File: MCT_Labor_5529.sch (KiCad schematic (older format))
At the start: 0 parts

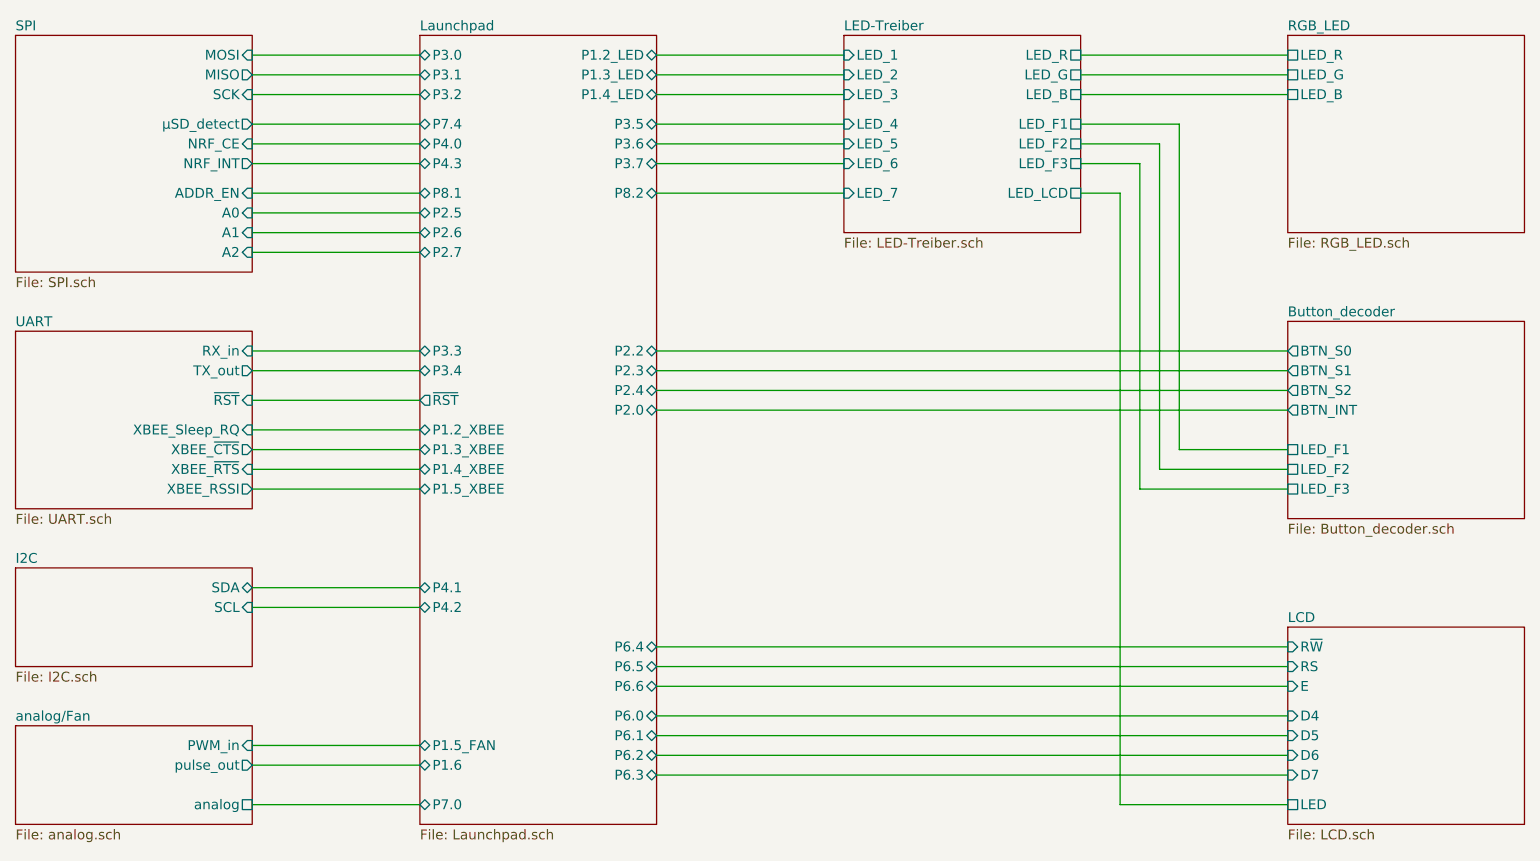
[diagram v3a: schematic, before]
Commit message: Anpassungen am Lüfteranschluss und den LEDs
-Lüfteranschluss verändert
 -> 12V-Versorgung eingefügt
-LED & LCD auf 3,3V umgestellt
 -> Ladungspunpe für neg. Kontrastspannung
-keine 5V Versorgung mehr
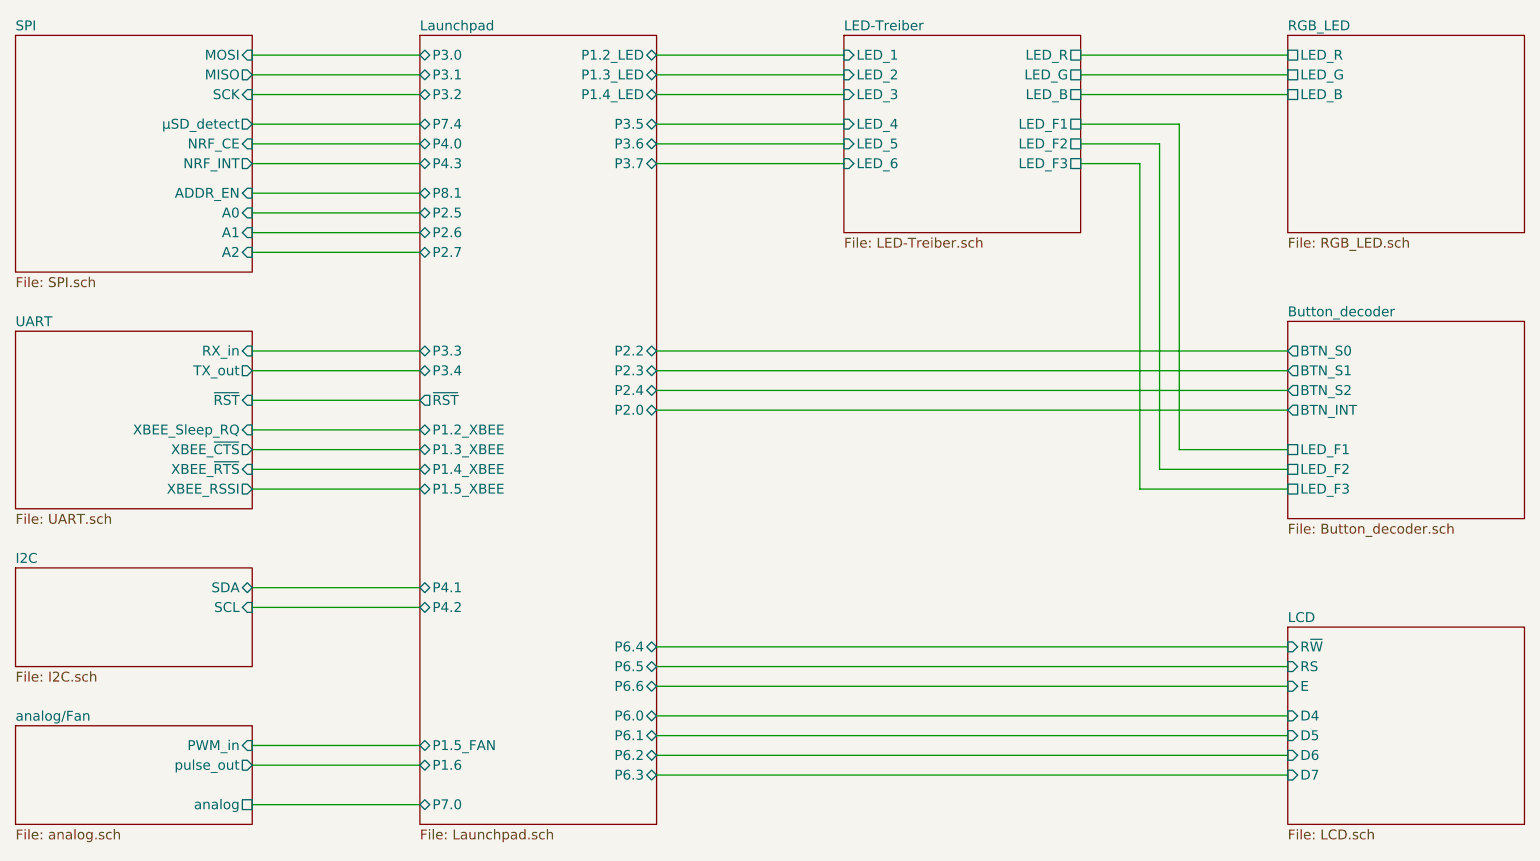
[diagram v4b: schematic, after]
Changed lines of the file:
@@
 F7 "R~W~" I L 8750 4650 50
 F8 "E" I L 8750 4850 50
-F9 "LED" U L 8750 5450 50
 $EndSheet
 Wire Wire Line
@@
 F6 "LED_5" I L 6500 2100 50
 F7 "LED_6" I L 6500 2200 50
-F8 "LED_7" I L 6500 2350 50
-F9 "LED_R" U R 7700 1650 50
-F10 "LED_G" U R 7700 1750 50
-F11 "LED_B" U R 7700 1850 50
-F12 "LED_F1" U R 7700 2000 50
-F13 "LED_F2" U R 7700 2100 50
-F14 "LED_F3" U R 7700 2200 50
-F15 "LED_LCD" U R 7700 2350 50
-$EndSheet
-Wire Wire Line
-	7700 2350 7900 2350
-Wire Wire Line
-	7900 2350 7900 5450
-Wire Wire Line
-	7900 5450 8750 5450
+F8 "LED_R" U R 7700 1650 50
+F9 "LED_G" U R 7700 1750 50
+F10 "LED_B" U R 7700 1850 50
+F11 "LED_F1" U R 7700 2000 50
+F12 "LED_F2" U R 7700 2100 50
+F13 "LED_F3" U R 7700 2200 50
+$EndSheet
 Wire Wire Line
 	6500 1650 5550 1650
@@
 Wire Wire Line
 	5550 2200 6500 2200
-Wire Wire Line
-	5550 2350 6500 2350
 $Sheet
 S 8750 3000 1200 1000
@@
 F14 "P4.0" B L 4350 2100 50
 F15 "P3.7" B R 5550 2200 50
-F16 "P8.2" B R 5550 2350 50
-F17 "P6.0" B R 5550 5000 50
-F18 "P6.1" B R 5550 5100 50
-F19 "P6.2" B R 5550 5200 50
-F20 "P6.3" B R 5550 5300 50
-F21 "P6.4" B R 5550 4650 50
-F22 "P7.0" B L 4350 5450 50
-F23 "P3.6" B R 5550 2100 50
-F24 "P3.5" B R 5550 2000 50
-F25 "P2.0" B R 5550 3450 50
-F26 "P2.2" B R 5550 3150 50
-F27 "P7.4" B L 4350 2000 50
-F28 "P3.0" B L 4350 1650 50
-F29 "P3.1" B L 4350 1750 50
-F30 "P2.6" B L 4350 2550 50
-F31 "P2.3" B R 5550 3250 50
-F32 "P8.1" B L 4350 2350 50
-F33 "~RST" O L 4350 3400 50
-F34 "P1.4_LED" B R 5550 1850 50
-F35 "P1.3_LED" B R 5550 1750 50
-F36 "P1.2_LED" B R 5550 1650 50
-F37 "P1.2_XBEE" B L 4350 3550 50
-F38 "P1.3_XBEE" B L 4350 3650 50
-F39 "P1.4_XBEE" B L 4350 3750 50
-F40 "P1.5_FAN" B L 4350 5150 50
-F41 "P1.5_XBEE" B L 4350 3850 50
-$EndSheet
-Wire Wire Line
+F16 "P6.0" B R 5550 5000 50
+F17 "P6.1" B R 5550 5100 50
+F18 "P6.2" B R 5550 5200 50
+F19 "P6.3" B R 5550 5300 50
+F20 "P6.4" B R 5550 4650 50
+F21 "P7.0" B L 4350 5450 50
+F22 "P3.6" B R 5550 2100 50
+F23 "P3.5" B R 5550 2000 50
+F24 "P2.0" B R 5550 3450 50
+F25 "P2.2" B R 5550 3150 50
+F26 "P7.4" B L 4350 2000 50
+F27 "P3.0" B L 4350 1650 50
+F28 "P3.1" B L 4350 1750 50
+F29 "P2.6" B L 4350 2550 50
+F30 "P2.3" B R 5550 3250 50
+F31 "P8.1" B L 4350 2350 50
+F32 "~RST" O L 4350 3400 50
+F33 "P1.4_LED" B R 5550 1850 50
+F34 "P1.3_LED" B R 5550 1750 50
+F35 "P1.2_LED" B R 5550 1650 50
+F36 "P1.2_XBEE" B L 4350 3550 50
+F37 "P1.3_XBEE" B L 4350 3650 50
+F38 "P1.4_XBEE" B L 4350 3750 50
+F39 "P1.5_FAN" B L 4350 5150 50
+F40 "P1.5_XBEE" B L 4350 3850 50
+$EndSheet
+Wire Wire Line

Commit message: minor glitches
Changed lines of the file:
@@
 F2 "RX_in" I R 3500 3150 50
 F3 "TX_out" O R 3500 3250 50
-F4 "~RST" I R 3500 3400 50
-F5 "XBEE_Sleep_RQ" I R 3500 3550 50
-F6 "XBEE_~CTS~" O R 3500 3650 50
-F7 "XBEE_~RTS~" I R 3500 3750 50
-F8 "XBEE_RSSI" O R 3500 3850 50
+F4 "XBEE_Sleep_RQ" I R 3500 3550 50
+F5 "XBEE_~CTS~" O R 3500 3650 50
+F6 "XBEE_~RTS~" I R 3500 3750 50
+F7 "XBEE_RSSI" O R 3500 3850 50
 $EndSheet
 $Sheet
@@
 F4 "analog" U R 3500 5450 50
 $EndSheet
-Wire Wire Line
-	4350 3400 3500 3400
 Wire Wire Line
 	4350 3150 3500 3150
@@
 F30 "P2.3" B R 5550 3250 50
 F31 "P8.1" B L 4350 2350 50
-F32 "~RST" O L 4350 3400 50
-F33 "P1.4_LED" B R 5550 1850 50
-F34 "P1.3_LED" B R 5550 1750 50
-F35 "P1.2_LED" B R 5550 1650 50
-F36 "P1.2_XBEE" B L 4350 3550 50
-F37 "P1.3_XBEE" B L 4350 3650 50
-F38 "P1.4_XBEE" B L 4350 3750 50
-F39 "P1.5_FAN" B L 4350 5150 50
-F40 "P1.5_XBEE" B L 4350 3850 50
+F32 "P1.4_LED" B R 5550 1850 50
+F33 "P1.3_LED" B R 5550 1750 50
+F34 "P1.2_LED" B R 5550 1650 50
+F35 "P1.2_XBEE" B L 4350 3550 50
+F36 "P1.3_XBEE" B L 4350 3650 50
+F37 "P1.4_XBEE" B L 4350 3750 50
+F38 "P1.5_FAN" B L 4350 5150 50
+F39 "P1.5_XBEE" B L 4350 3850 50
 $EndSheet
 Wire Wire Line
